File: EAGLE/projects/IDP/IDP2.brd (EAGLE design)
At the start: 100 x 80 mm, 8 parts, among them J1 22-05-7038-03, J2 22-05-7048-04, M1 IDP_PROTOBOARD, Q1 TEPT4400

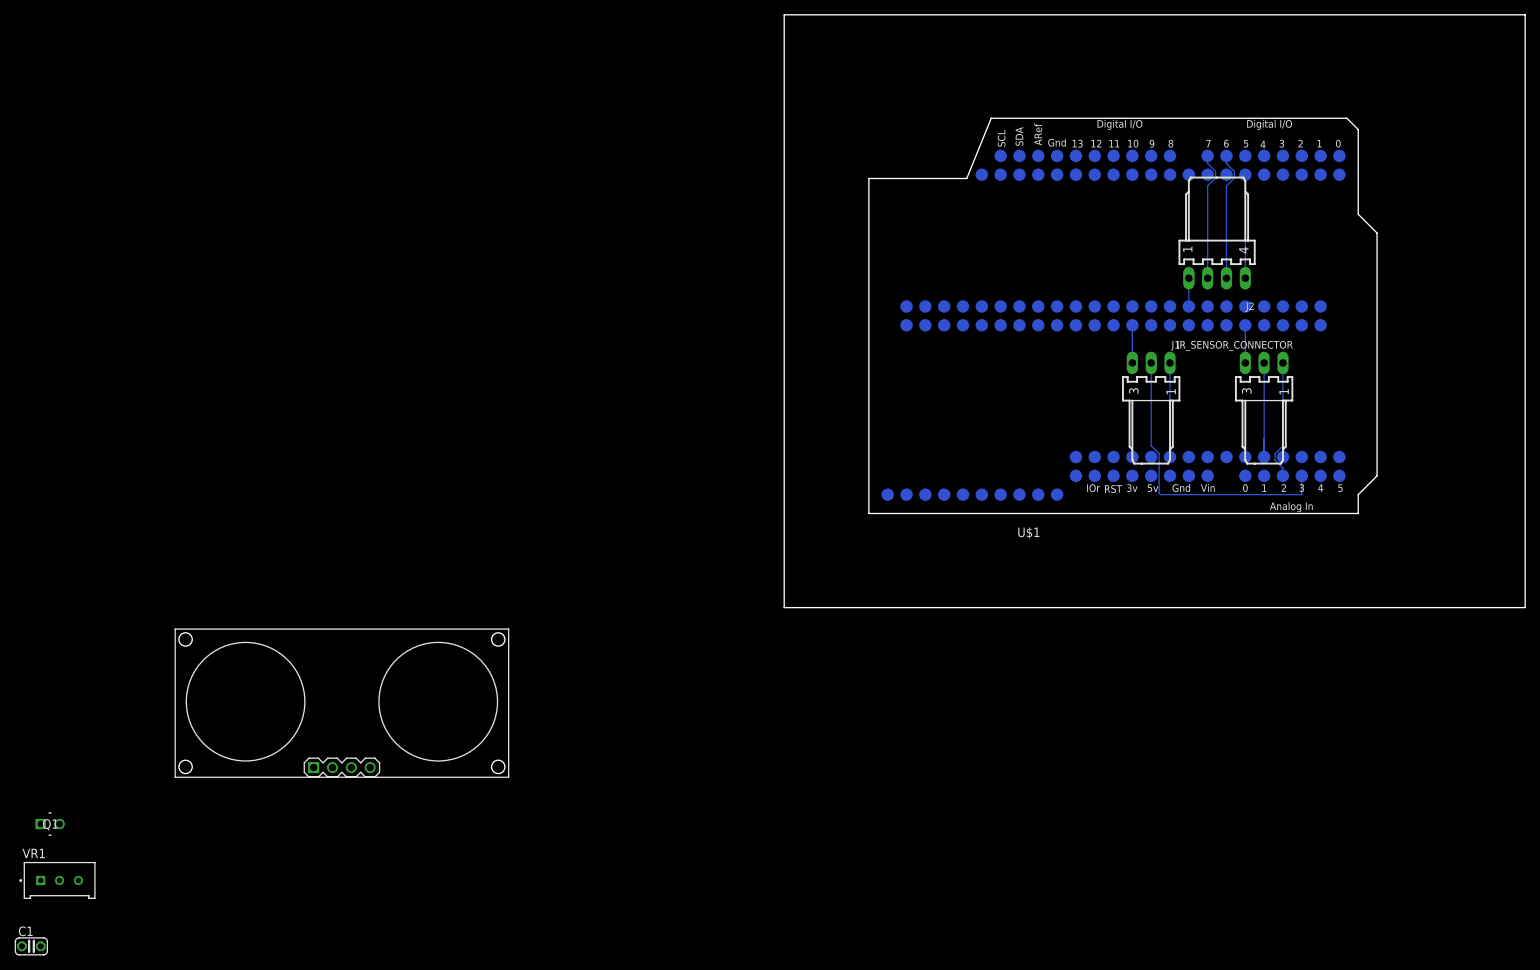
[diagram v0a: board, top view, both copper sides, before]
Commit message: Include Servo and Change Phototransistor Layout
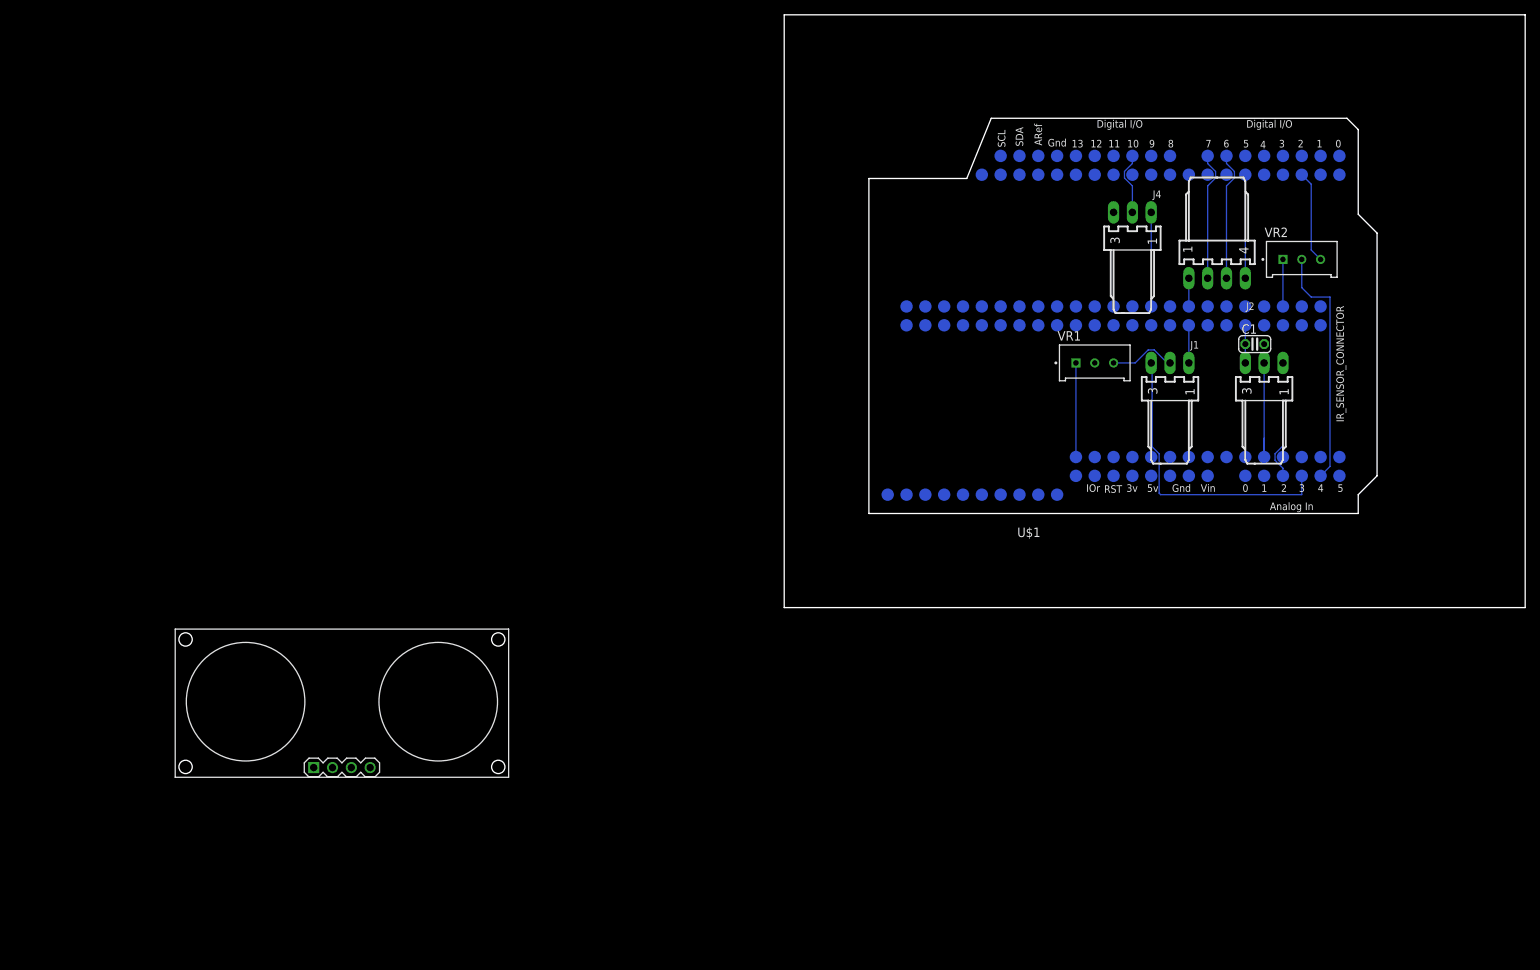
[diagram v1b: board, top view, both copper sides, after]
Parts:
- removed Q1: TEPT4400, TEPT4400:TEPT4400
- added J4: 22-05-7038-03, IDP_library:7395-03
- added VR2: POT, IDP_library:TRIM_3296W-1-250
- VR1: value 10k -> POT
- moved C1 184.0 mm to (62.2, 35.6)
- moved VR1 156.2 mm to (41.9, 33.0)
- moved J1 2.54 mm to (52.1, 33.0)
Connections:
- new net N$1: J1.2, VR1.3
- new net SERVO_ANALOG: M1.A4, VR2.2
- new net SERVO_PULSE: J4.2, M1.D10
- new net VCC: J4.3
- net +5V: now also J1.1, VR2.3; no longer J1.3, Q1.2
- net GND: now also J4.1, VR2.1; no longer J1.1
- net PHOTOTRANSISTOR: now also J1.3; no longer J1.2, Q1.1, VR1.3
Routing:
- net SERVO_ANALOG: track 0.00 -> 32.8 mm
- net GND: track 31.8 -> 50.8 mm
- net +5V: track 22.9 -> 35.3 mm
- net IR_SENSOR_VALUES: track 16.1 -> 4.93 mm
- net N$1: track 0.00 -> 9.07 mm
- net SERVO_PULSE: track 0.00 -> 8.50 mm

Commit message: Added Part Names
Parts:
- removed U$1: ULTRASONIC-HC-SR04, diy-modules:ULTRASONIC-HC-SR04
- IR_SENSOR_CONNECTOR, PHOTOTRANSISTOR, SERVO: value 22-05-7038-03 -> Rapid 22-1010 / 22-0910
- RAPID65-0753, RAPID68-1959: value POT -> 10K
- ULTRASONIC_SENSOR: value 22-05-7048-04 -> Rapid 22-1015/22-0915
- renumbered J1 to PHOTOTRANSISTOR, J2 to ULTRASONIC_SENSOR, J4 to SERVO, VR1 to RAPID65-0753, VR2 to RAPID68-1959
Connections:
- net +5V: no longer U$1.1
- net ECHO: no longer U$1.3
- net GND: no longer U$1.4
- net TRIG: no longer U$1.2
